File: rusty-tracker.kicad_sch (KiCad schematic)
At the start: 166 parts, among them J1 SIM8051-6-0-14-01-X, J2 USB_C_Receptacle_USB2.0, J3 NFC, J4 tag-connect-swd, J5 Battery Connector, Q1 BC846, Q2 BC846, SW1 SW_Push, T1 Tab, T2 Tab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

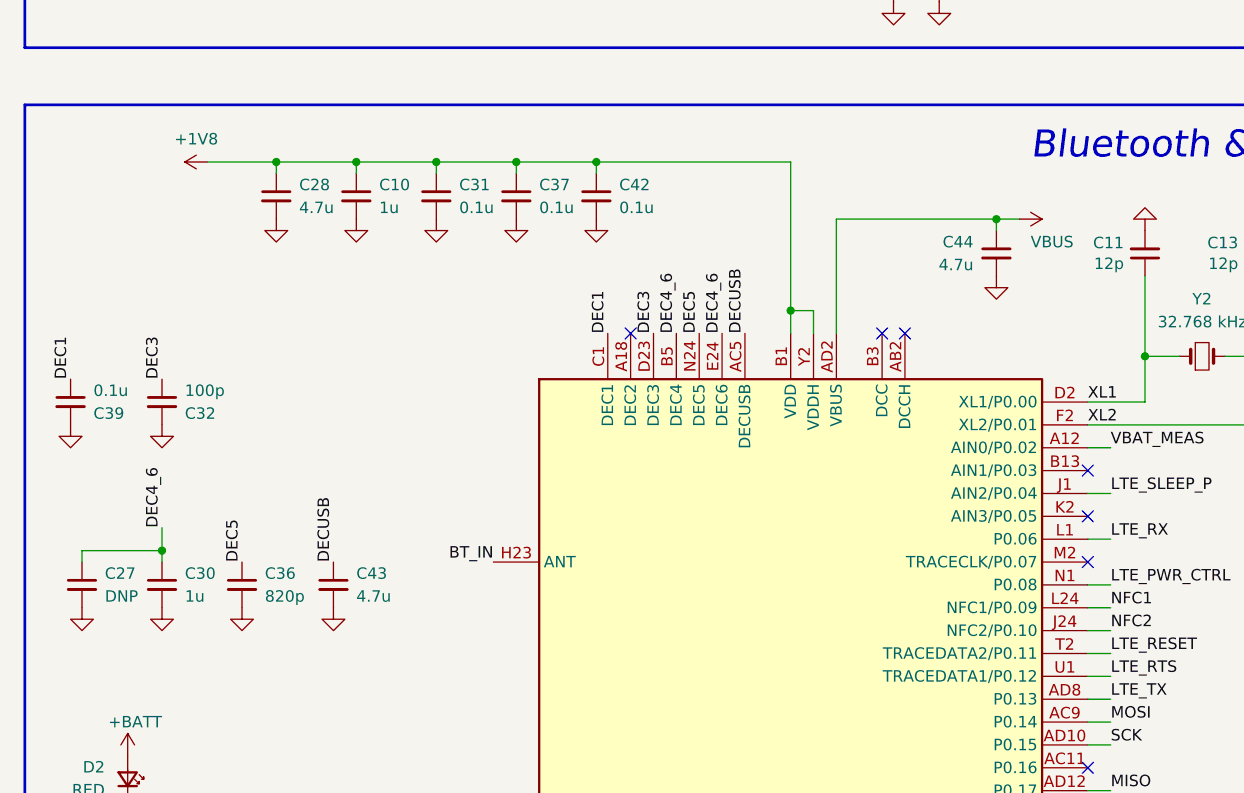
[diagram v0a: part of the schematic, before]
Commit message: Add support for VBAT -> VDDH, and DCDC for the nRF52840
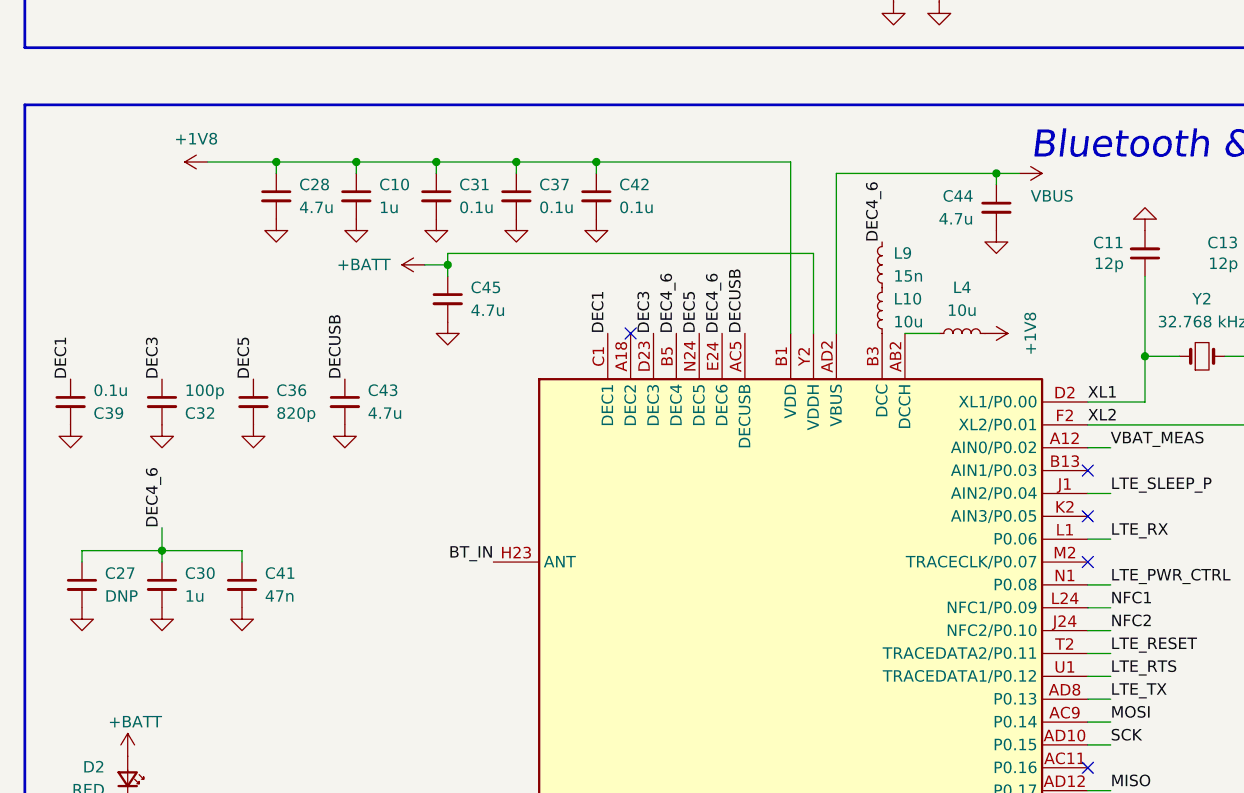
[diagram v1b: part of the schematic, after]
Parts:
- added C41: 47n, passive:C_0402, symbol Device:C_Small
- added C45: 4.7u, passive:C_0402, symbol Device:C_Small
- added L10, L4: 10u, passive:R_0603, symbol Device:L_Small
- added L9: 15n, passive:R_0402, symbol Device:L_Small
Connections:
- net +1V8: now also L4.1; no longer U2.Y2 (VDDH)
- net +BATT: now also U2.Y2 (VDDH), C45.1
- net DEC4_6: now also C41.1, L9.1
- net GND: now also C41.2, C45.2
- net at U2.AB2 (DCCH): now also L4.2
- net at U2.B3 (DCC): now also L10.2
- new net: L10.1, L9.2
- no-connect marks 60 -> 58
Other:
- moved on the sheet: C36, C43, C44

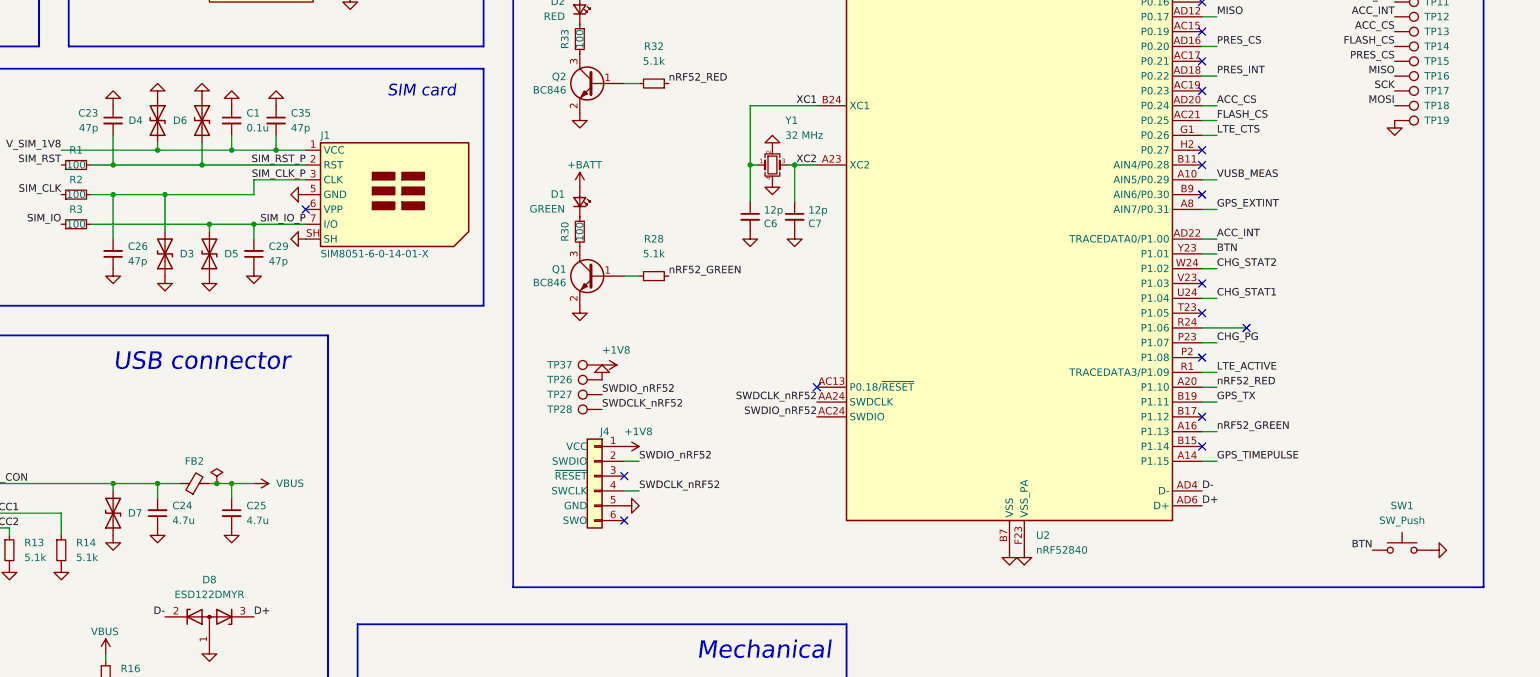
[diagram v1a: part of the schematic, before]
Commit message: Add protection & debounce to button
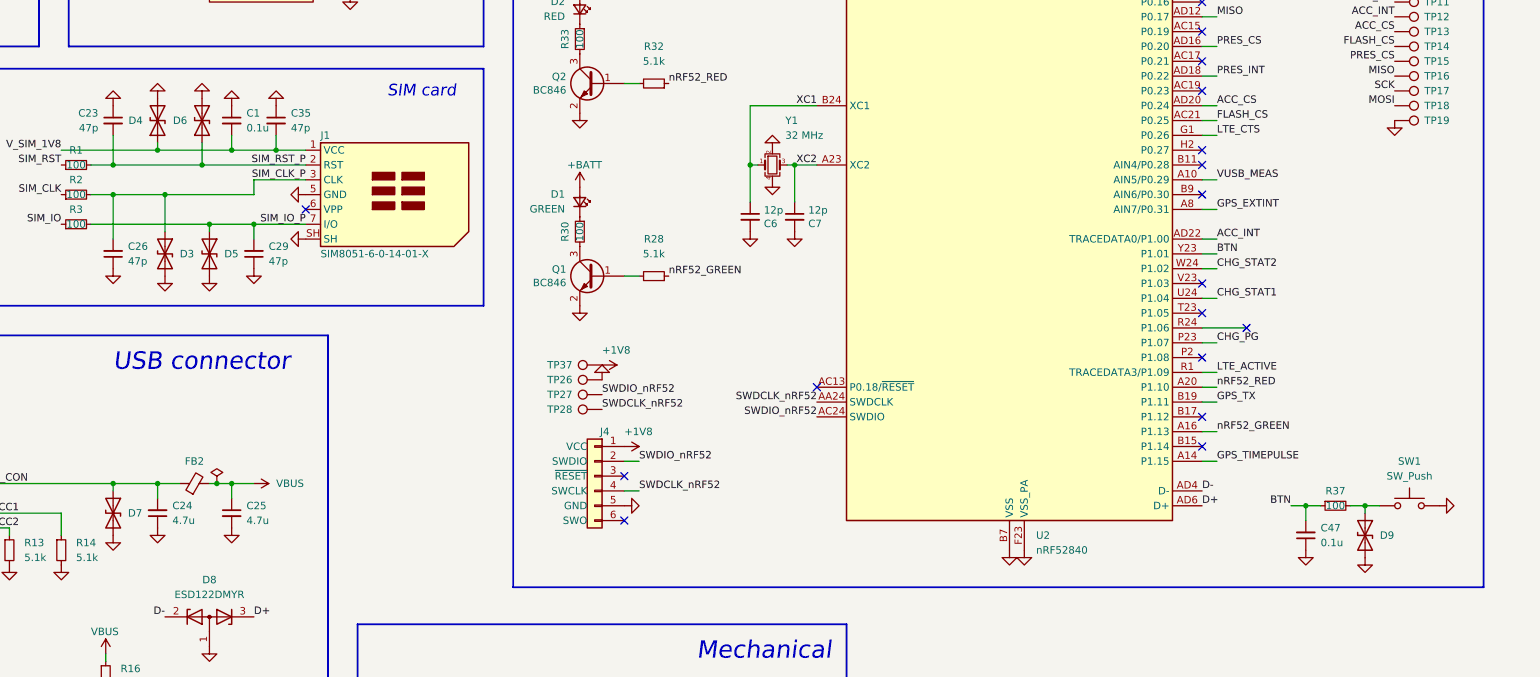
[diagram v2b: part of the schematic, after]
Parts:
- added C47: 0.1u, passive:C_0402, symbol Device:C_Small
- added D9: D_TVS, passive:D_0402_DFN1006, symbol Device:D_TVS
- added R37: 100, passive:R_0402, symbol Device:R_Small
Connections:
- net BTN: now also C47.2, R37.1; no longer SW1.1
- net GND: now also D3.2 (A2), D4.2 (A2), D5.2 (A2), D6.2 (A2), D7.2 (A2), C47.1, D9.2 (A2); no longer D3.1 (A1), D4.1 (A1), D5.1 (A1), D6.1 (A1), D7.1 (A1)
- net SIM_CLK_P: now also D3.1 (A1); no longer D3.2 (A2)
- net SIM_IO_P: now also D5.1 (A1); no longer D5.2 (A2)
- net SIM_RST_P: now also D6.1 (A1); no longer D6.2 (A2)
- net VBUS_CON: now also D7.1 (A1); no longer D7.2 (A2)
- net V_SIM_1V8: now also D4.1 (A1); no longer D4.2 (A2)
- new net: D9.1 (A1), R37.2, SW1.1
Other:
- moved on the sheet: D3, D4, D5, D6, D7, SW1

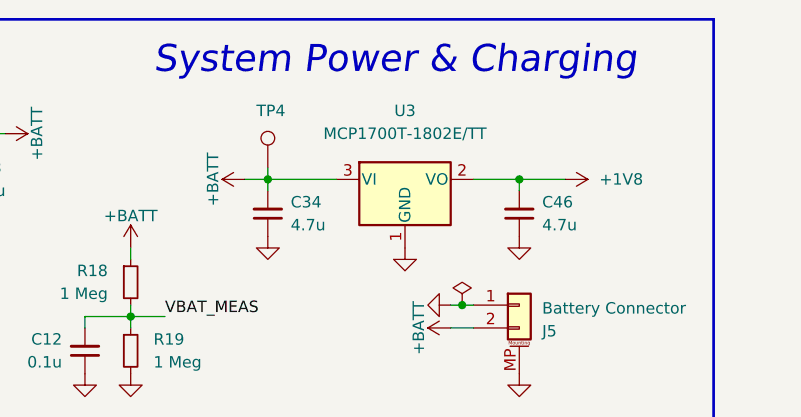
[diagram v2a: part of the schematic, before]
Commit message: Make LDO DNP
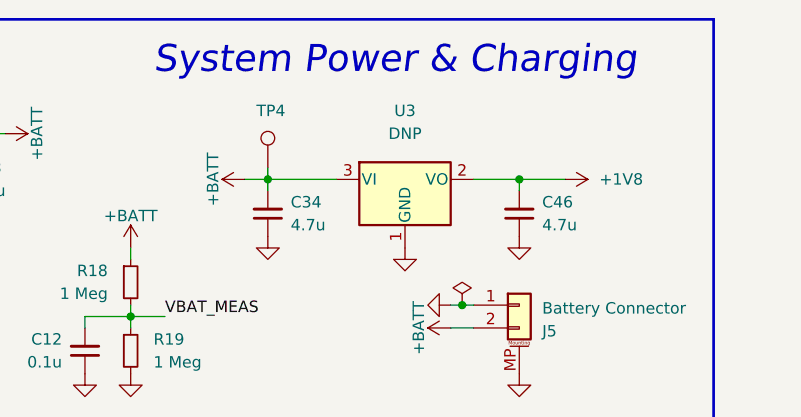
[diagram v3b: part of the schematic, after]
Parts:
- U3: value MCP1700T-1802E/TT -> DNP; MFPN (none) -> MCP1700T-1802E/TT
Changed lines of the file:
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@@
     (in_bom yes) (on_board yes) (fields_autoplaced)
     (property "Reference" "U3" (id 0) (at 367.03 25.4 0))
-    (property "Value" "MCP1700T-1802E/TT" (id 1) (at 367.03 27.94 0))
+    (property "Value" "DNP" (id 1) (at 367.03 27.94 0))
     (property "Footprint" "Package_TO_SOT_SMD:SOT-23" (id 2) (at 367.03 27.305 0)
       (effects (font (size 1.27 1.27)) hide)
@@
       (effects (font (size 1.27 1.27)) hide)
     )
+    (property "MFPN" "MCP1700T-1802E/TT" (id 4) (at 367.03 33.02 0)
+      (effects (font (size 1.27 1.27)) hide)
+    )
     (pin "1")
     (pin "2")
@@
     )
     (path "/3a834b9f-6950-4124-8f0a-7e667c6838b4"
-      (reference "U3") (unit 1) (value "MCP1700T-1802E/TT") (footprint "Package_TO_SOT_SMD:SOT-23")
+      (reference "U3") (unit 1) (value "DNP") (footprint "Package_TO_SOT_SMD:SOT-23")
     )
     (path "/d437bf96-ac28-4f1d-9f7b-def64e871b88"

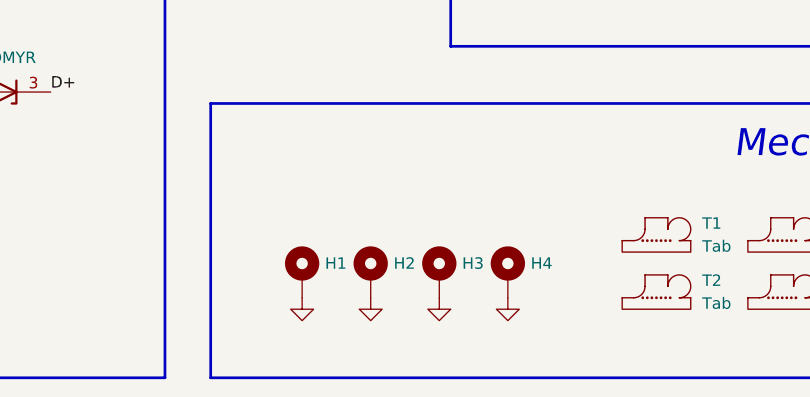
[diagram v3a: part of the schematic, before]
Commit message: Remove GND connection in screws
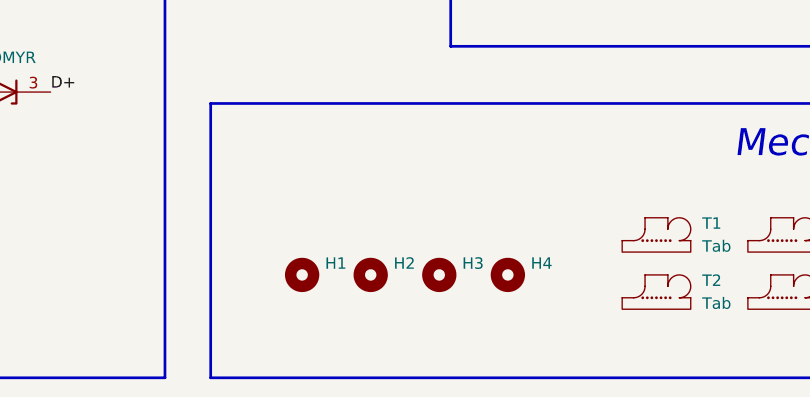
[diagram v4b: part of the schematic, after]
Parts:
- H1, H2, H3, H4: footprint MountingHole:MountingHole_2.2mm_M2_Pad_Via -> MountingHole:MountingHole_2.2mm_M2; symbol Mechanical:MountingHole_Pad -> Mechanical:MountingHole
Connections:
- net GND: no longer H1.1, H2.1, H3.1, H4.1
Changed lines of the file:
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@@
     (pin "1")
   )
-  (symbol (lib_id "Mechanical:MountingHole_Pad") (at 218.44 265.43 0) (unit 1)
+  (symbol (lib_id "Mechanical:MountingHole") (at 218.44 265.43 0) (unit 1)
     (in_bom yes) (on_board yes) (fields_autoplaced)
     (property "Reference" "H1" (id 0) (at 220.98 264.1599 0)
@@
       (effects (font (size 1.27 1.27)) (justify left) hide)
     )
-    (property "Footprint" "MountingHole:MountingHole_2.2mm_M2_Pad_Via" (id 2) (at 218.44 265.43 0)
+    (property "Footprint" "MountingHole:MountingHole_2.2mm_M2" (id 2) (at 218.44 265.43 0)
       (effects (font (size 1.27 1.27)) hide)
     )
@@
       (effects (font (size 1.27 1.27)) hide)
     )
-    (pin "1")
   )
   (symbol (lib_id "power:GND") (at 128.27 173.99 0) (unit 1)
@@
     (pin "2")
   )
-  (symbol (lib_id "power:GND") (at 218.44 267.97 0) (unit 1)
-    (in_bom yes) (on_board yes) (fields_autoplaced)
-    (property "Reference" "#PWR014" (id 0) (at 218.44 274.32 0)
-      (effects (font (size 1.27 1.27)) hide)
-    )
-    (property "Value" "GND" (id 1) (at 218.4399 271.78 90)
-      (effects (font (size 1.27 1.27)) (justify right) hide)
-    )
-    (property "Footprint" "" (id 2) (at 218.44 267.97 0)
-      (effects (font (size 1.27 1.27)) hide)
-    )
-    (property "Datasheet" "" (id 3) (at 218.44 267.97 0)
-      (effects (font (size 1.27 1.27)) hide)
-    )
-    (pin "1")
-  )
   (symbol (lib_id "power:+BATT") (at 372.11 49.53 90) (mirror x) (unit 1)
     (in_bom yes) (on_board yes) (fields_autoplaced)
@@
     (pin "1")
   )
-  (symbol (lib_id "power:GND") (at 226.06 267.97 0) (unit 1)
-    (in_bom yes) (on_board yes) (fields_autoplaced)
-    (property "Reference" "#PWR045" (id 0) (at 226.06 274.32 0)
-      (effects (font (size 1.27 1.27)) hide)
-    )
-    (property "Value" "GND" (id 1) (at 226.0599 271.78 90)
-      (effects (font (size 1.27 1.27)) (justify right) hide)
-    )
-    (property "Footprint" "" (id 2) (at 226.06 267.97 0)
-      (effects (font (size 1.27 1.27)) hide)
-    )
-    (property "Datasheet" "" (id 3) (at 226.06 267.97 0)
-      (effects (font (size 1.27 1.27)) hide)
-    )
-    (pin "1")
-  )
   (symbol (lib_id "Device:C_Small") (at 372.11 82.55 0) (mirror x) (unit 1)
     (in_bom yes) (on_board yes)
@@
     (pin "1")
   )
-  (symbol (lib_id "power:GND") (at 233.68 267.97 0) (unit 1)
-    (in_bom yes) (on_board yes) (fields_autoplaced)
-    (property "Reference" "#PWR046" (id 0) (at 233.68 274.32 0)
-      (effects (font (size 1.27 1.27)) hide)
-    )
-    (property "Value" "GND" (id 1) (at 233.6799 271.78 90)
-      (effects (font (size 1.27 1.27)) (justify right) hide)
-    )
-    (property "Footprint" "" (id 2) (at 233.68 267.97 0)
-      (effects (font (size 1.27 1.27)) hide)
-    )
-    (property "Datasheet" "" (id 3) (at 233.68 267.97 0)
-      (effects (font (size 1.27 1.27)) hide)
-    )
-    (pin "1")
-  )
   (symbol (lib_id "Device:D_Zener_Dual_CommonAnode_AKK") (at 182.88 245.11 0) (unit 1)
     (in_bom yes) (on_board yes) (fields_autoplaced)
@@
     (pin "1")
   )
-  (symbol (lib_id "power:GND") (at 241.3 267.97 0) (unit 1)
-    (in_bom yes) (on_board yes) (fields_autoplaced)
-    (property "Reference" "#PWR049" (id 0) (at 241.3 274.32 0)
-      (effects (font (size 1.27 1.27)) hide)
-    )
-    (property "Value" "GND" (id 1) (at 241.2999 271.78 90)
-      (effects (font (size 1.27 1.27)) (justify right) hide)
-    )
-    (property "Footprint" "" (id 2) (at 241.3 267.97 0)
-      (effects (font (size 1.27 1.27)) hide)
-    )
-    (property "Datasheet" "" (id 3) (at 241.3 267.97 0)
-      (effects (font (size 1.27 1.27)) hide)
-    )
-    (pin "1")
-  )
   (symbol (lib_id "Connector:TestPoint") (at 53.34 85.09 90) (unit 1)
     (in_bom no) (on_board yes)
@@
     (pin "2")
   )
-  (symbol (lib_id "Mechanical:MountingHole_Pad") (at 241.3 265.43 0) (unit 1)
+  (symbol (lib_id "Mechanical:MountingHole") (at 241.3 265.43 0) (unit 1)
     (in_bom yes) (on_board yes) (fields_autoplaced)
     (property "Reference" "H4" (id 0) (at 243.84 264.1599 0)
@@
       (effects (font (size 1.27 1.27)) (justify left) hide)
     )
-    (property "Footprint" "MountingHole:MountingHole_2.2mm_M2_Pad_Via" (id 2) (at 241.3 265.43 0)
+    (property "Footprint" "MountingHole:MountingHole_2.2mm_M2" (id 2) (at 241.3 265.43 0)
       (effects (font (size 1.27 1.27)) hide)
     )
@@
       (effects (font (size 1.27 1.27)) hide)
     )
-    (pin "1")
   )
   (symbol (lib_id "power:GND") (at 250.19 204.47 0) (mirror x) (unit 1)
@@
     (pin "2")
   )
-  (symbol (lib_id "Mechanical:MountingHole_Pad") (at 233.68 265.43 0) (unit 1)
+  (symbol (lib_id "Mechanical:MountingHole") (at 233.68 265.43 0) (unit 1)
     (in_bom yes) (on_board yes) (fields_autoplaced)
     (property "Reference" "H3" (id 0) (at 236.22 264.1599 0)
@@
       (effects (font (size 1.27 1.27)) (justify left) hide)
     )
-    (property "Footprint" "MountingHole:MountingHole_2.2mm_M2_Pad_Via" (id 2) (at 233.68 265.43 0)
+    (property "Footprint" "MountingHole:MountingHole_2.2mm_M2" (id 2) (at 233.68 265.43 0)
       (effects (font (size 1.27 1.27)) hide)
     )
@@
       (effects (font (size 1.27 1.27)) hide)
     )
-    (pin "1")
   )
   (symbol (lib_id "Device:C_Small") (at 67.31 219.71 0) (unit 1)
@@
     )
   )
-  (symbol (lib_id "Mechanical:MountingHole_Pad") (at 226.06 265.43 0) (unit 1)
+  (symbol (lib_id "Mechanical:MountingHole") (at 226.06 265.43 0) (unit 1)
     (in_bom yes) (on_board yes) (fields_autoplaced)
     (property "Reference" "H2" (id 0) (at 228.6 264.1599 0)
@@
       (effects (font (size 1.27 1.27)) (justify left) hide)
     )
-    (property "Footprint" "MountingHole:MountingHole_2.2mm_M2_Pad_Via" (id 2) (at 226.06 265.43 0)
+    (property "Footprint" "MountingHole:MountingHole_2.2mm_M2" (id 2) (at 226.06 265.43 0)
       (effects (font (size 1.27 1.27)) hide)
     )
@@
       (effects (font (size 1.27 1.27)) hide)
     )
-    (pin "1")
   )
   (symbol (lib_id "Device:R_Small") (at 95.25 229.87 180) (unit 1)
@@
       (reference "#PWR013") (unit 1) (value "GND") (footprint "")
     )
-    (path "/1c46d123-4719-4bca-bd78-7b90291fe771"
-      (reference "#PWR014") (unit 1) (value "GND") (footprint "")
-    )
     (path "/2f380c9f-032c-4814-bf2e-9db688c67345"
       (reference "#PWR015") (unit 1) (value "GND") (footprint "")
@@
       (reference "#PWR044") (unit 1) (value "GND") (footprint "")
     )
-    (path "/337f3395-45f6-483d-acdf-5a0e6a10941b"
-      (reference "#PWR045") (unit 1) (value "GND") (footprint "")
-    )
-    (path "/4f78220d-681c-4726-9346-2485eaf32cb5"
-      (reference "#PWR046") (unit 1) (value "GND") (footprint "")
-    )
     (path "/62f7188c-245e-4aa4-b12f-e664dff069c5"
       (reference "#PWR047") (unit 1) (value "GND") (footprint "")
@@
       (reference "#PWR048") (unit 1) (value "GND") (footprint "")
     )
-    (path "/6b949bea-5ac4-451f-a40b-8a86d67838b4"
-      (reference "#PWR049") (unit 1) (value "GND") (footprint "")
-    )
     (path "/06e0028c-44ed-44f6-bb83-bd2e7cc53ec1"
       (reference "#PWR050") (unit 1) (value "GND") (footprint "")
@@
     )
     (path "/19ac343d-501c-4e09-a054-92326a70f9fd"
-      (reference "H1") (unit 1) (value "MountingHole_Pad") (footprint "MountingHole:MountingHole_2.2mm_M2_Pad_Via")
+      (reference "H1") (unit 1) (value "MountingHole_Pad") (footprint "MountingHole:MountingHole_2.2mm_M2")
     )
     (path "/d8441b3b-f8d8-4acf-b6be-75540c3f0517"
-      (reference "H2") (unit 1) (value "MountingHole_Pad") (footprint "MountingHole:MountingHole_2.2mm_M2_Pad_Via")
+      (reference "H2") (unit 1) (value "MountingHole_Pad") (footprint "MountingHole:MountingHole_2.2mm_M2")
     )
     (path "/cc4a7f39-b3f4-40b0-a8b5-de441d0f28d5"
-      (reference "H3") (unit 1) (value "MountingHole_Pad") (footprint "MountingHole:MountingHole_2.2mm_M2_Pad_Via")
+      (reference "H3") (unit 1) (value "MountingHole_Pad") (footprint "MountingHole:MountingHole_2.2mm_M2")
     )
     (path "/b45c24d6-1b21-4428-885c-618a6afea5ed"
-      (reference "H4") (unit 1) (value "MountingHole_Pad") (footprint "MountingHole:MountingHole_2.2mm_M2_Pad_Via")
+      (reference "H4") (unit 1) (value "MountingHole_Pad") (footprint "MountingHole:MountingHole_2.2mm_M2")
     )
     (path "/f492245f-1457-4df1-b407-bf6295a3ea32"
